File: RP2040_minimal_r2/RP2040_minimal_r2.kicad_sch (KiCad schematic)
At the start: 43 parts, among them J1 SPI0.6, J10 B22, J11 B23, J12 Breakout, J2 SPI0.8, J3 SPI1.13, J4 I2C0, J5 USB, J6 B18, J7 B19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

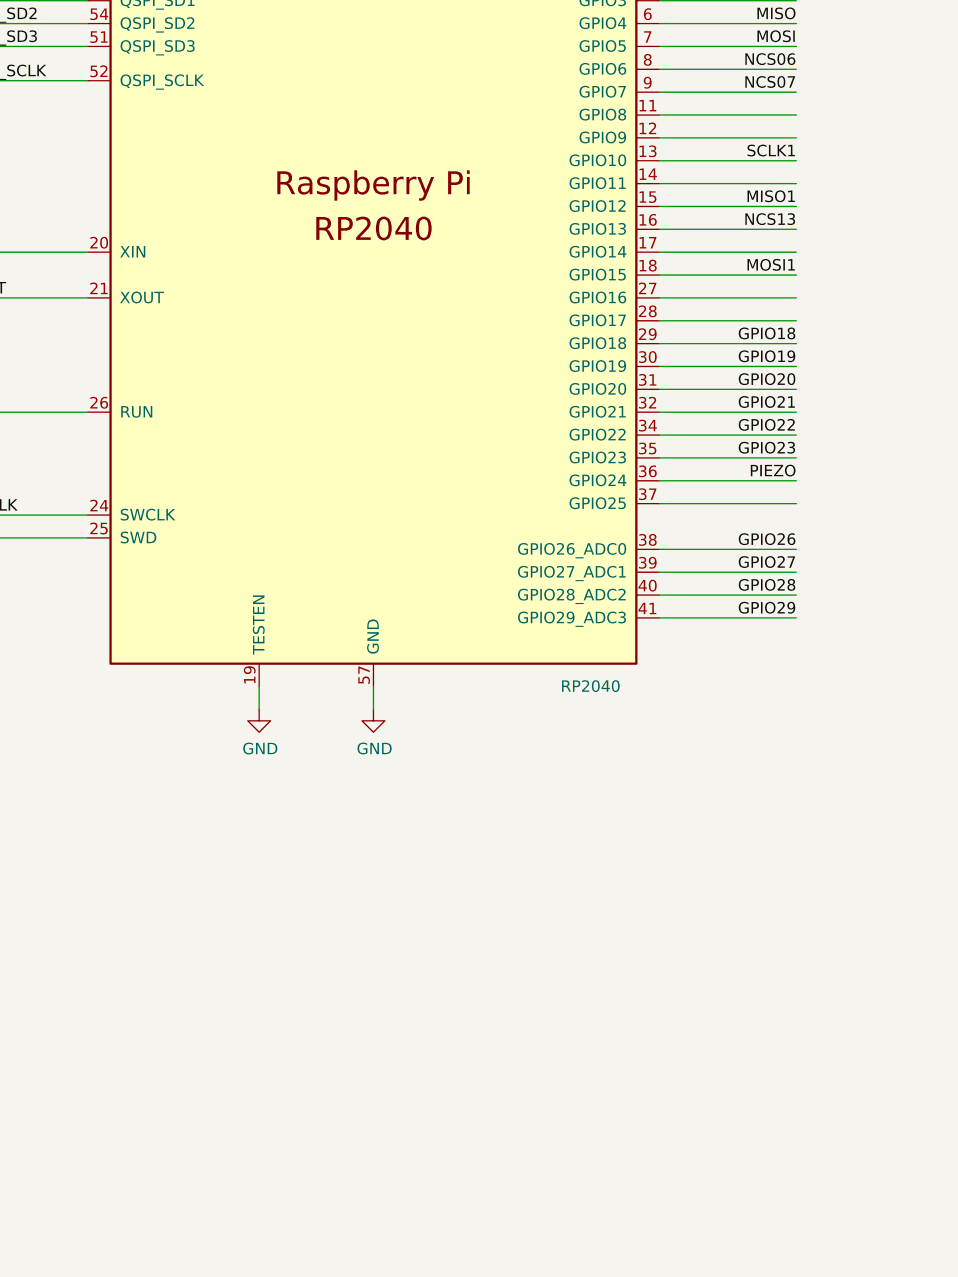
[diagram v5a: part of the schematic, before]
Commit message: Added a WS2812 LED (a.k.a. NeoPixel) Removed some top-side ground traces in favor of vias closer to ground pads. Updated the github URL. Minor changes to the readme.
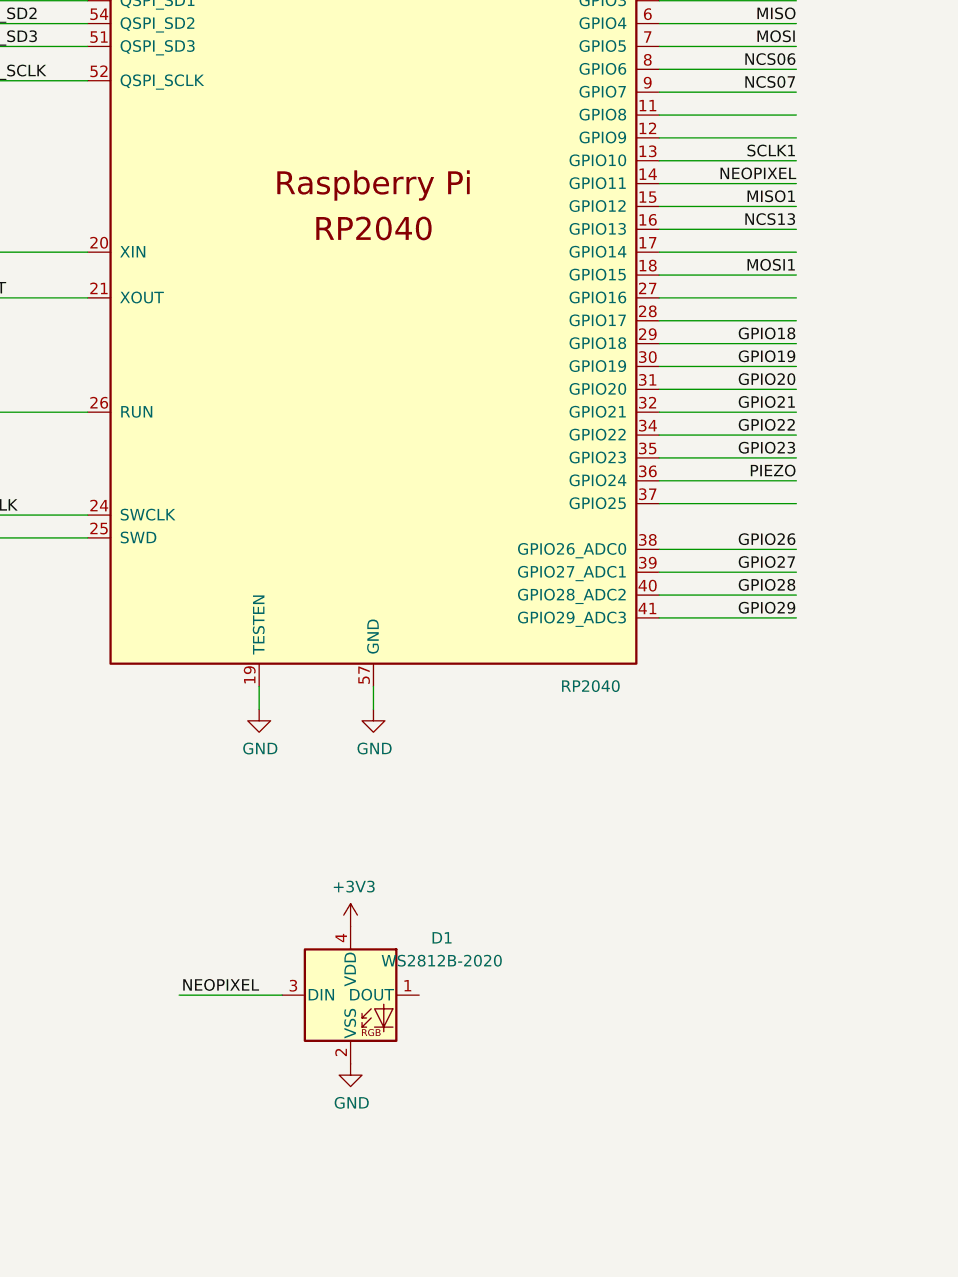
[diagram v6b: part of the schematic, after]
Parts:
- added D1: WS2812B-2020, LED_SMD:LED_WS2812B-2020_PLCC4_2.0x2.0mm, symbol LED:WS2812B-2020
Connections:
- net +3V3: now also D1.4 (VDD)
- net GND: now also D1.2 (VSS)
- net NEOPIXEL: now reaches U3.14 (GPIO11)
- net NEOPIXEL: now also D1.3 (DIN)
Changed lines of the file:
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@@
 	(wire
 		(pts
+			(xy 176.53 229.87) (xy 187.96 229.87)
+		)
+		(stroke
+			(width 0)
+			(type default)
+		)
+	)
+	(wire
+		(pts
 			(xy 97.79 101.6) (xy 97.79 105.41)
 		)
@@
 		)
 	)
+	(label "NEOPIXEL"
+		(at 245.11 139.7 180)
+		(fields_autoplaced yes)
+		(effects
+			(font
+				(size 1.27 1.27)
+			)
+			(justify right bottom)
+		)
+	)
 	(label "QSPI_SS"
 		(at 71.12 125.73 0)
@@
 		)
 	)
+	(label "NEOPIXEL"
+		(at 185.42 229.87 180)
+		(fields_autoplaced yes)
+		(effects
+			(font
+				(size 1.27 1.27)
+			)
+			(justify right bottom)
+		)
+	)
 	(label "NCS06"
 		(at 245.11 127 180)
@@
 	)
 	(symbol
+		(lib_id "power:GND")
+		(at 195.58 237.49 0)
+		(unit 1)
+		(exclude_from_sim no)
+		(in_bom yes)
+		(on_board yes)
+		(dnp no)
+		(property "Reference" "#PWR043"
+			(at 195.58 243.84 0)
+			(effects
+				(font
+					(size 1.27 1.27)
+				)
+				(hide yes)
+			)
+		)
+		(property "Value" "GND"
+			(at 195.707 241.8842 0)
+			(effects
+				(font
+					(size 1.27 1.27)
+				)
+			)
+		)
+		(property "Footprint" ""
+			(at 195.58 237.49 0)
+			(effects
+				(font
+					(size 1.27 1.27)
+				)
+				(hide yes)
+			)
+		)
+		(property "Datasheet" ""
+			(at 195.58 237.49 0)
+			(effects
+				(font
+					(size 1.27 1.27)
+				)
+				(hide yes)
+			)
+		)
+		(property "Description" ""
+			(at 195.58 237.49 0)
+			(effects
+				(font
+					(size 1.27 1.27)
+				)
+				(hide yes)
+			)
+		)
+		(pin "1"
+		)
+		(instances
+			(project "RP2040_minimal_r2"
+				(path "/8c0b3d8b-46d3-4173-ab1e-a61765f77d61"
+					(reference "#PWR043")
+					(unit 1)
+				)
+			)
+		)
+	)
+	(symbol
 		(lib_id "Trackball-rescue:PWR_FLAG-power")
 		(at 121.92 52.07 180)
@@
 	)
 	(symbol
+		(lib_id "PMW3360-rescue:+3V3-power")
+		(at 195.58 222.25 0)
+		(unit 1)
+		(exclude_from_sim no)
+		(in_bom yes)
+		(on_board yes)
+		(dnp no)
+		(property "Reference" "#PWR044"
+			(at 195.58 226.06 0)
+			(effects
+				(font
+					(size 1.27 1.27)
+				)
+				(hide yes)
+			)
+		)
+		(property "Value" "+3V3"
+			(at 195.961 217.8558 0)
+			(effects
+				(font
+					(size 1.27 1.27)
+				)
+			)
+		)
+		(property "Footprint" ""
+			(at 195.58 222.25 0)
+			(effects
+				(font
+					(size 1.27 1.27)
+				)
+				(hide yes)
+			)
+		)
+		(property "Datasheet" ""
+			(at 195.58 222.25 0)
+			(effects
+				(font
+					(size 1.27 1.27)
+				)
+				(hide yes)
+			)
+		)
+		(property "Description" ""
+			(at 195.58 222.25 0)
+			(effects
+				(font
+					(size 1.27 1.27)
+				)
+				(hide yes)
+			)
+		)
+		(pin "1"
+		)
+		(instances
+			(project "RP2040_minimal_r2"
+				(path "/8c0b3d8b-46d3-4173-ab1e-a61765f77d61"
+					(reference "#PWR044")
+					(unit 1)
+				)
+			)
+		)
+	)
+	(symbol
 		(lib_id "Connector_Generic:Conn_01x04")
 		(at 350.52 140.97 0)
@@
 					(unit 1)
 				)
+			)
+		)
+	)
+	(symbol
+		(lib_id "LED:WS2812B-2020")
+		(at 195.58 229.87 0)
+		(unit 1)
+		(exclude_from_sim no)
+		(in_bom yes)
+		(on_board yes)
+		(dnp no)
+		(fields_autoplaced yes)
+		(property "Reference" "D1"
+			(at 205.74 223.5514 0)
+			(effects
+				(font
+					(size 1.27 1.27)
+				)
+			)
+		)
+		(property "Value" "WS2812B-2020"
+			(at 205.74 226.0914 0)
+			(effects
+				(font
+					(size 1.27 1.27)
+				)
+			)
+		)
+		(property "Footprint" "LED_SMD:LED_WS2812B-2020_PLCC4_2.0x2.0mm"
+			(at 196.85 237.49 0)
+			(effects
+				(font
+					(size 1.27 1.27)
+				)
+				(justify left top)
+				(hide yes)
+			)
+		)
+		(property "Datasheet" "https://jlcpcb.com/api/file/downloadByFileSystemAccessId/8552950702205911040"
+			(at 198.12 239.395 0)
+			(effects
+				(font
+					(size 1.27 1.27)
+				)
+				(justify left top)
+				(hide yes)
+			)
+		)
+		(property "Description" "RGB LED with integrated controller, 2.0 x 2.0 mm, 12 mA"
+			(at 195.58 229.87 0)
+			(effects
+				(font
+					(size 1.27 1.27)
+				)
+				(hide yes)
+			)
+		)
+		(property "LCSC" "C965555"
+			(at 195.58 229.87 0)
+			(effects
+				(font
+					(size 1.27 1.27)
+				)
+				(hide yes)
+			)
+		)
+		(pin "1"
+		)
+		(pin "3"
+		)
+		(pin "4"
+		)
+		(pin "2"
+		)
+		(instances
+			(project ""
+				(path "/8c0b3d8b-46d3-4173-ab1e-a61765f77d61"
+					(reference "D1")
+					(unit 1)
+				)
